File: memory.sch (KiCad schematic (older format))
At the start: 1 part

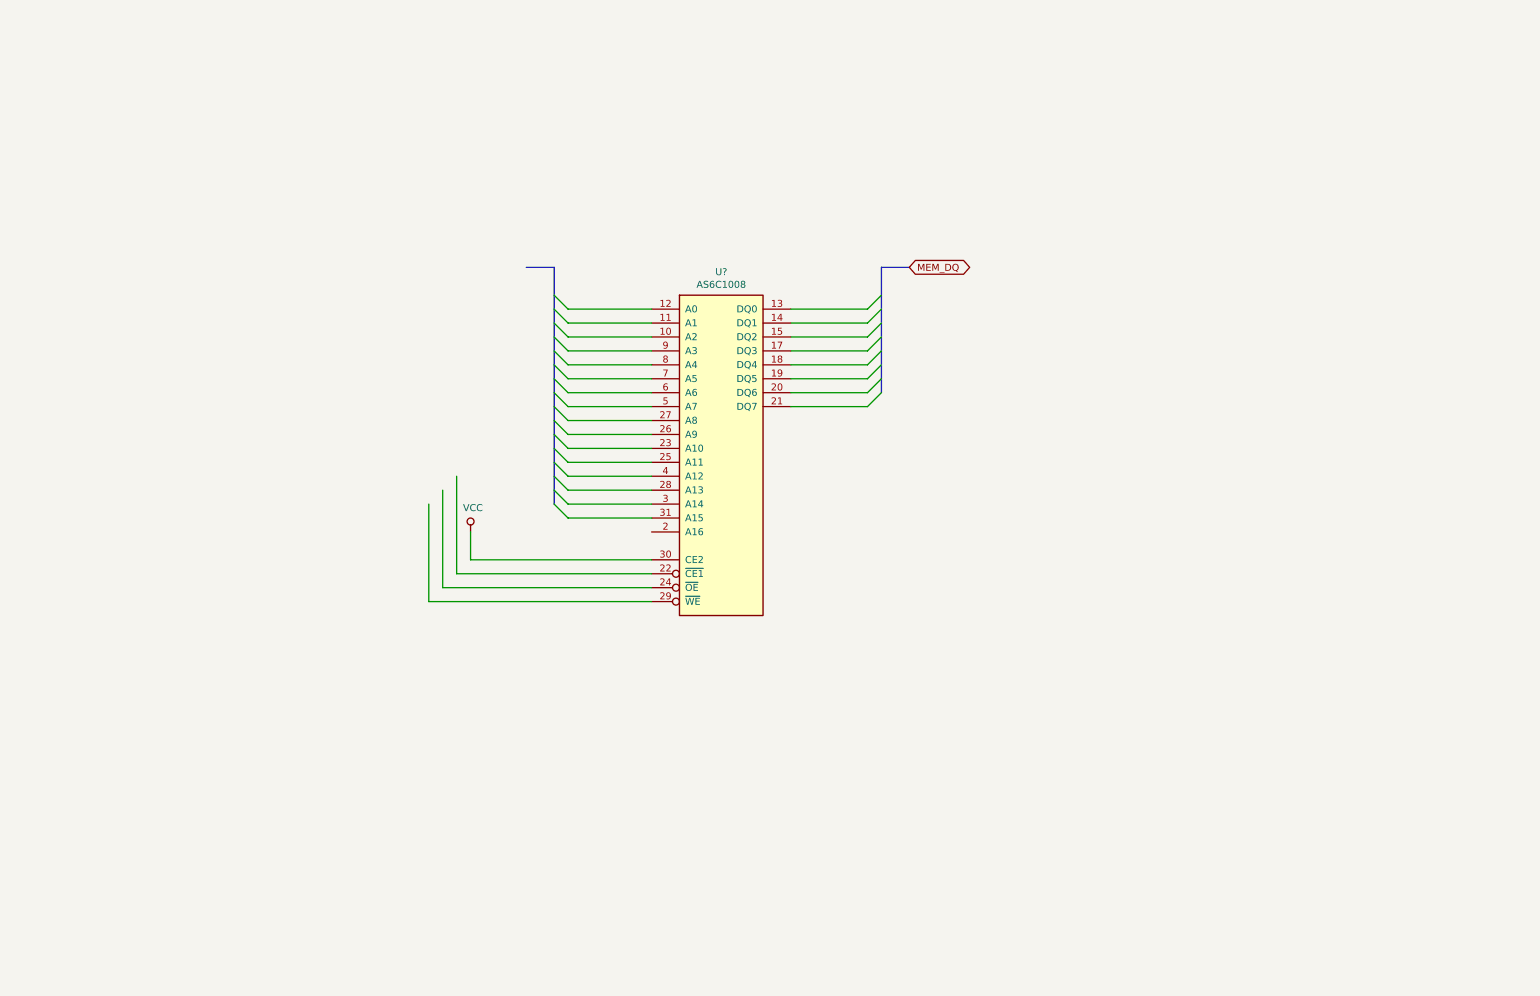
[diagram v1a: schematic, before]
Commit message: created mux part
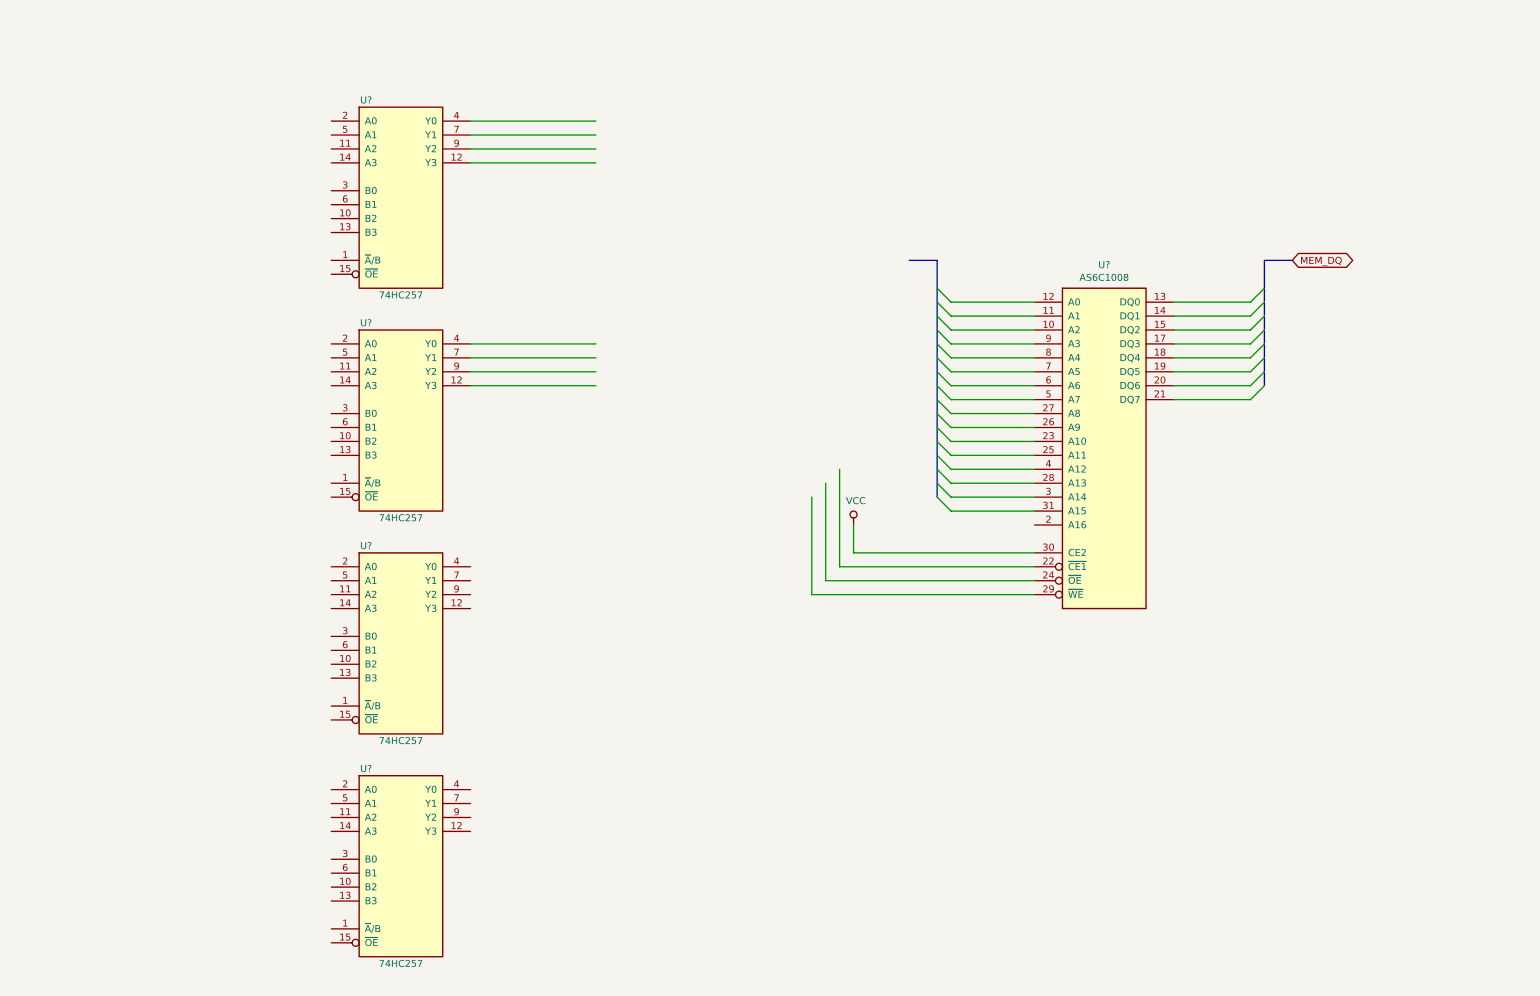
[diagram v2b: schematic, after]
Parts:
- added U? (x4): 74HC257, symbol 74xx_modified:74LS257
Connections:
- wire segments 32 -> 40
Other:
- moved on the sheet: U?
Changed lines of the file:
@@
 $Descr A4 11693 8268
 encoding utf-8
-Sheet 5 6
+Sheet 4 6
 Title ""
 Date ""
@@
 L 74xx_modified:AS6C1008 U?
 U 1 1 5CBBFD35
-P 5500 3350
-F 0 "U?" H 5500 4167 50  0000 C CNN
-F 1 "AS6C1008" H 5500 4076 50  0000 C CNN
-F 2 "" H 5450 3350 50  0001 C CNN
-F 3 "" H 5450 3350 50  0001 C CNN
-	1    5500 3350
-	1    0    0    -1
-$EndComp
-Wire Wire Line
-	6000 2800 6550 2800
-Wire Wire Line
-	6000 2900 6550 2900
-Wire Wire Line
-	6000 3000 6550 3000
-Wire Wire Line
-	6000 3100 6550 3100
-Wire Wire Line
-	6000 3200 6550 3200
-Wire Wire Line
-	6000 3300 6550 3300
-Wire Wire Line
-	6000 3400 6550 3400
-Wire Wire Line
-	6000 3500 6550 3500
-Entry Wire Line
-	6550 2800 6650 2700
-Entry Wire Line
-	6550 2900 6650 2800
-Entry Wire Line
-	6550 3000 6650 2900
-Entry Wire Line
-	6550 3100 6650 3000
-Entry Wire Line
-	6550 3200 6650 3100
-Entry Wire Line
-	6550 3300 6650 3200
-Entry Wire Line
-	6550 3400 6650 3300
-Entry Wire Line
-	6550 3500 6650 3400
-Wire Bus Line
-	6650 2500 6850 2500
-Text GLabel 6850 2500 2    50   BiDi ~ 0
+P 8250 3300
+F 0 "U?" H 8250 4117 50  0000 C CNN
+F 1 "AS6C1008" H 8250 4026 50  0000 C CNN
+F 2 "" H 8200 3300 50  0001 C CNN
+F 3 "" H 8200 3300 50  0001 C CNN
+	1    8250 3300
+	1    0    0    -1
+$EndComp
+Wire Wire Line
+	8750 2750 9300 2750
+Wire Wire Line
+	8750 2850 9300 2850
+Wire Wire Line
+	8750 2950 9300 2950
+Wire Wire Line
+	8750 3050 9300 3050
+Wire Wire Line
+	8750 3150 9300 3150
+Wire Wire Line
+	8750 3250 9300 3250
+Wire Wire Line
+	8750 3350 9300 3350
+Wire Wire Line
+	8750 3450 9300 3450
+Entry Wire Line
+	9300 2750 9400 2650
+Entry Wire Line
+	9300 2850 9400 2750
+Entry Wire Line
+	9300 2950 9400 2850
+Entry Wire Line
+	9300 3050 9400 2950
+Entry Wire Line
+	9300 3150 9400 3050
+Entry Wire Line
+	9300 3250 9400 3150
+Entry Wire Line
+	9300 3350 9400 3250
+Entry Wire Line
+	9300 3450 9400 3350
+Wire Bus Line
+	9400 2450 9600 2450
+Text GLabel 9600 2450 2    50   BiDi ~ 0
 MEM_DQ
 Wire Bus Line
-	4300 2500 4100 2500
-Entry Wire Line
-	4300 4200 4400 4300
-Entry Wire Line
-	4300 4100 4400 4200
-Entry Wire Line
-	4300 4000 4400 4100
-Entry Wire Line
-	4300 3900 4400 4000
-Entry Wire Line
-	4300 3800 4400 3900
-Entry Wire Line
-	4300 3700 4400 3800
-Entry Wire Line
-	4300 3600 4400 3700
-Entry Wire Line
-	4300 3500 4400 3600
-Entry Wire Line
-	4300 3400 4400 3500
-Entry Wire Line
-	4300 3300 4400 3400
-Entry Wire Line
-	4300 3200 4400 3300
-Entry Wire Line
-	4300 3100 4400 3200
-Entry Wire Line
-	4300 3000 4400 3100
-Entry Wire Line
-	4300 2900 4400 3000
-Entry Wire Line
-	4300 2800 4400 2900
-Entry Wire Line
-	4300 2700 4400 2800
-Wire Wire Line
-	4400 2800 5000 2800
-Wire Wire Line
-	4400 2900 5000 2900
-Wire Wire Line
-	4400 3000 5000 3000
-Wire Wire Line
-	4400 3100 5000 3100
-Wire Wire Line
-	4400 3200 5000 3200
-Wire Wire Line
-	4400 3300 5000 3300
-Wire Wire Line
-	4400 3400 5000 3400
-Wire Wire Line
-	4400 3500 5000 3500
-Wire Wire Line
-	4400 3600 5000 3600
-Wire Wire Line
-	4400 3700 5000 3700
-Wire Wire Line
-	4400 3800 5000 3800
-Wire Wire Line
-	4400 3900 5000 3900
-Wire Wire Line
-	4400 4000 5000 4000
-Wire Wire Line
-	4400 4100 5000 4100
-Wire Wire Line
-	4400 4200 5000 4200
-Wire Wire Line
-	4400 4300 5000 4300
-Wire Wire Line
-	5000 4600 3700 4600
-Wire Wire Line
-	3700 4600 3700 4400
-Wire Wire Line
-	5000 4700 3600 4700
-Wire Wire Line
-	3600 4700 3600 4000
-Wire Wire Line
-	5000 4800 3500 4800
-Wire Wire Line
-	3500 4800 3500 4100
-Wire Wire Line
-	5000 4900 3400 4900
-Wire Wire Line
-	3400 4900 3400 4200
-Wire Bus Line
-	6650 2500 6650 3400
-Wire Bus Line
-	4300 2500 4300 4200
+	7050 2450 6850 2450
+Entry Wire Line
+	7050 4150 7150 4250
+Entry Wire Line
+	7050 4050 7150 4150
+Entry Wire Line
+	7050 3950 7150 4050
+Entry Wire Line
+	7050 3850 7150 3950
+Entry Wire Line
+	7050 3750 7150 3850
+Entry Wire Line
+	7050 3650 7150 3750
+Entry Wire Line
+	7050 3550 7150 3650
+Entry Wire Line
+	7050 3450 7150 3550
+Entry Wire Line
+	7050 3350 7150 3450
+Entry Wire Line
+	7050 3250 7150 3350
+Entry Wire Line
+	7050 3150 7150 3250
+Entry Wire Line
+	7050 3050 7150 3150
+Entry Wire Line
+	7050 2950 7150 3050
+Entry Wire Line
+	7050 2850 7150 2950
+Entry Wire Line
+	7050 2750 7150 2850
+Entry Wire Line
+	7050 2650 7150 2750
+Wire Wire Line
+	7150 2750 7750 2750
+Wire Wire Line
+	7150 2850 7750 2850
+Wire Wire Line
+	7150 2950 7750 2950
+Wire Wire Line
+	7150 3050 7750 3050
+Wire Wire Line
+	7150 3150 7750 3150
+Wire Wire Line
+	7150 3250 7750 3250
+Wire Wire Line
+	7150 3350 7750 3350
+Wire Wire Line
+	7150 3450 7750 3450
+Wire Wire Line
+	7150 3550 7750 3550
+Wire Wire Line
+	7150 3650 7750 3650
+Wire Wire Line
+	7150 3750 7750 3750
+Wire Wire Line
+	7150 3850 7750 3850
+Wire Wire Line
+	7150 3950 7750 3950
+Wire Wire Line
+	7150 4050 7750 4050
+Wire Wire Line
+	7150 4150 7750 4150
+Wire Wire Line
+	7150 4250 7750 4250
+Wire Wire Line
+	7750 4550 6450 4550
+Wire Wire Line
+	6450 4550 6450 4350
+Wire Wire Line
+	7750 4650 6350 4650
+Wire Wire Line
+	6350 4650 6350 3950
+Wire Wire Line
+	7750 4750 6250 4750
+Wire Wire Line
+	6250 4750 6250 4050
+Wire Wire Line
+	7750 4850 6150 4850
+Wire Wire Line
+	6150 4850 6150 4150
 $Comp
 L power:VCC #PWR?
 U 1 1 5CBC2B7B
-P 3700 4400
-F 0 "#PWR?" H 3700 4250 50  0001 C CNN
-F 1 "VCC" H 3717 4573 50  0000 C CNN
-F 2 "" H 3700 4400 50  0001 C CNN
-F 3 "" H 3700 4400 50  0001 C CNN
-	1    3700 4400
-	1    0    0    -1
-$EndComp
+P 6450 4350
+F 0 "#PWR?" H 6450 4200 50  0001 C CNN
+F 1 "VCC" H 6467 4523 50  0000 C CNN
+F 2 "" H 6450 4350 50  0001 C CNN
+F 3 "" H 6450 4350 50  0001 C CNN
+	1    6450 4350
+	1    0    0    -1
+$EndComp
+$Comp
+L 74xx_modified:74LS257 U?
+U 1 1 5C55466F
+P 3200 2050
+F 0 "U?" H 2950 2800 50  0000 C CNN
+F 1 "74HC257" H 3200 1400 50  0000 C CNN
+F 2 "" H 3200 2050 50  0001 C CNN
+F 3 "http://www.ti.com/lit/gpn/sn74LS257" H 3200 2050 50  0001 C CNN
+	1    3200 2050
+	1    0    0    -1
+$EndComp
+$Comp
+L 74xx_modified:74LS257 U?
+U 1 1 5C5601F9
+P 3200 3650
+F 0 "U?" H 2950 4400 50  0000 C CNN
+F 1 "74HC257" H 3200 3000 50  0000 C CNN
+F 2 "" H 3200 3650 50  0001 C CNN
+F 3 "http://www.ti.com/lit/gpn/sn74LS257" H 3200 3650 50  0001 C CNN
+	1    3200 3650
+	1    0    0    -1
+$EndComp
+$Comp
+L 74xx_modified:74LS257 U?
+U 1 1 5C5602CB
+P 3200 5250
+F 0 "U?" H 2950 6000 50  0000 C CNN
+F 1 "74HC257" H 3200 4600 50  0000 C CNN
+F 2 "" H 3200 5250 50  0001 C CNN
+F 3 "http://www.ti.com/lit/gpn/sn74LS257" H 3200 5250 50  0001 C CNN
+	1    3200 5250
+	1    0    0    -1
+$EndComp
+$Comp
+L 74xx_modified:74LS257 U?
+U 1 1 5C560317
+P 3200 6850
+F 0 "U?" H 2950 7600 50  0000 C CNN
+F 1 "74HC257" H 3200 6200 50  0000 C CNN
+F 2 "" H 3200 6850 50  0001 C CNN
+F 3 "http://www.ti.com/lit/gpn/sn74LS257" H 3200 6850 50  0001 C CNN
+	1    3200 6850
+	1    0    0    -1
+$EndComp
+Wire Wire Line
+	3700 1450 4600 1450
+Wire Wire Line
+	3700 1550 4600 1550
+Wire Wire Line
+	3700 1650 4600 1650
+Wire Wire Line
+	3700 1750 4600 1750
+Wire Wire Line
+	3700 3050 4600 3050
+Wire Bus Line
+	9400 2450 9400 3350
+Wire Bus Line
+	7050 2450 7050 4150
+Wire Wire Line
+	3700 3150 4600 3150
+Wire Wire Line
+	3700 3250 4600 3250
+Wire Wire Line
+	3700 3350 4600 3350
 $EndSCHEMATC

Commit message: mem muxing done
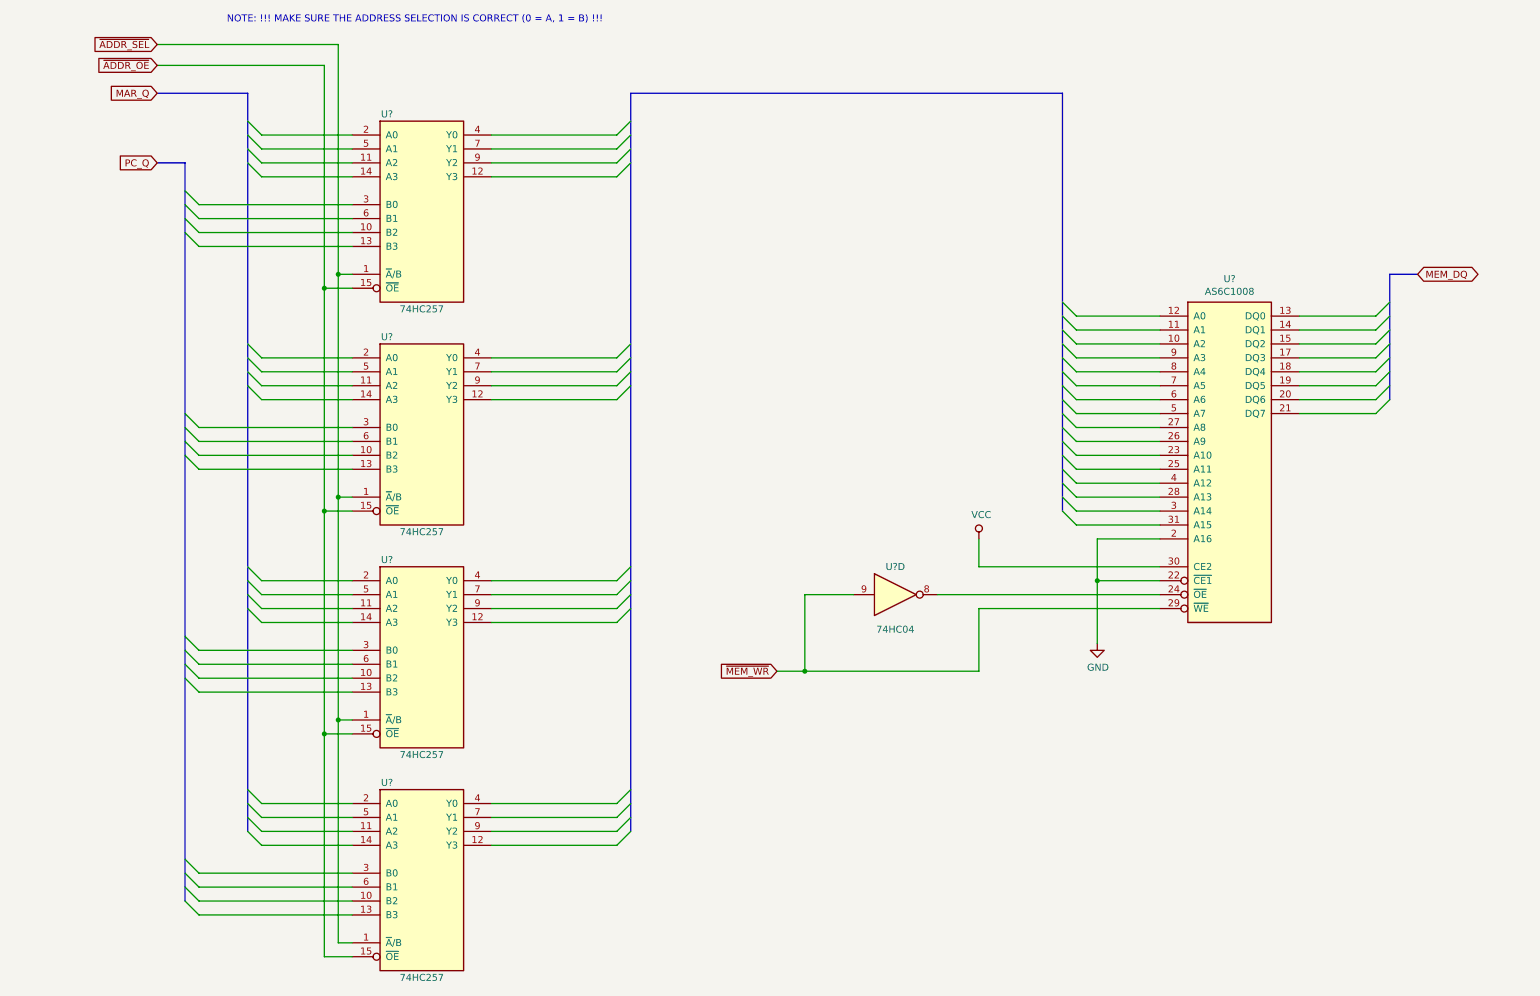
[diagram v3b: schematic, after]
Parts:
- added U?: 74HC04, Package_DIP:DIP-14_W7.62mm, symbol 74xx:74LS04
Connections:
- net labels added: GND, MAR_Q, PC_Q, ~ADDR_OE, ~ADDR_SEL, ~MEM_WR
- wire segments 40 -> 103
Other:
- note added: "NOTE: !!! MAKE SURE THE ADDRESS SELECTION IS CORRECT (0 = A, 1 = B) !!!"
- moved on the sheet: U?
